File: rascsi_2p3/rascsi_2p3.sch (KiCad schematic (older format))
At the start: 90 parts, among them IC1 SN74LS641-1DW, IC2 SN74LS641-1DW, IC3 SN74LS641-1DW, IC4 SN74LS641-1DW, J1 Raspberry_Pi_2_3, J2 Conn_01x02_Male, J3 Conn_02x25_Odd_Even, J4 I2C Pinout, J5 Conn_02x03_Odd_Even, J6 CONNFLY DB-25, J7 Conn_01x02_Male, X1 Mac, X2 Dogcow, X3 Mac, X4 Dogcow, X5 Dogcow, X6 Dogcow, X7 Pi, X8 Pi

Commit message: Commit ordered version of the board
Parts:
- D1, D2, D3, D4: Description (none) -> Generic 0805 Green LED
- H1, H2, H3, H4, H5, H6: Description (none) -> N/A - Mounting Hole; Height (none) -> N/A; LCSC (none) -> N/A; Manufacturer_Name (none) -> N/A; Manufacturer_Part_Number (none) -> N/A; Mouser Part Number (none) -> N/A; Mouser Price/Stock (none) -> N/A
- IC1, IC2, IC3, IC4: footprint SOIC127P1030X265-20N -> SamacSys_Parts:SOIC127P1030X265-20N
- J2, J7: value Conn_01x02_Male -> DNP; Description (none) -> DNP; Height (none) -> DNP; LCSC C2337 -> DNP; Manufacturer_Name (none) -> DNP; Manufacturer_Part_Number (none) -> DNP; Mouser Part Number (none) -> DNP; Mouser Price/Stock (none) -> DNP
- J3: Description (none) -> 2.54mm 2x25 pin Box Header; Manufacturer_Name (none) -> TE Connectivity; Manufacturer_Part_Number (none) -> 3-1761603-5; Mouser Part Number (none) -> 571-3-1761603-5; Mouser Price/Stock (none) -> https://www.mouser.com/ProductDetail/TE-Connectivity/3-1761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
- J4: Description (none) -> Generic 1x5 2.5mm pin socket; Manufacturer_Name (none) -> Harwin; Manufacturer_Part_Number (none) -> M20-7820546; Mouser Part Number (none) -> 855-M20-7820546; Mouser Price/Stock (none) -> https://www.mouser.com/ProductDetail/Harwin/M20-7820546?qs=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
- J5: value Conn_02x03_Odd_Even -> DNP; Description (none) -> DNP; Height (none) -> DNP; LCSC C3409 -> DNP; Manufacturer_Name (none) -> DNP; Manufacturer_Part_Number (none) -> DNP; Mouser Part Number (none) -> DNP; Mouser Price/Stock (none) -> DNP
- J6: footprint L717SDB25PA4CH4F -> SamacSys_Parts:L717SDB25PA4CH4F
- R1, R10, R11, R12, R13, R14, R15, R16, R17, R18, R19, R2, R20, R21, R22, R23, R24, R25, R26, R27, R28, R29, R3, R30, R31, R32, R33, R34, R35, R36, R37, R38, R39, R4, R40, R41, R42, R43, R44, R45, R46, R47, R48, R49, R5, R50, R51, R52, R53, R54, R55, R56, R57, R58, R6, R7, R8, R9: footprint Resistor_SMD:R_0402_1005Metric -> Resistor_THT:R_Axial_DIN0204_L3.6mm_D1.6mm_P1.90mm_Vertical
- X1, X2, X3, X4, X5, X6, X7, X8: Description (none) -> N/A - Silkscreen; Height (none) -> N/A; LCSC (none) -> N/A; Manufacturer_Name (none) -> N/A; Manufacturer_Part_Number (none) -> N/A; Mouser Part Number (none) -> N/A; Mouser Price/Stock (none) -> N/A
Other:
- note added: "2.3a"
- note removed: "2.3"

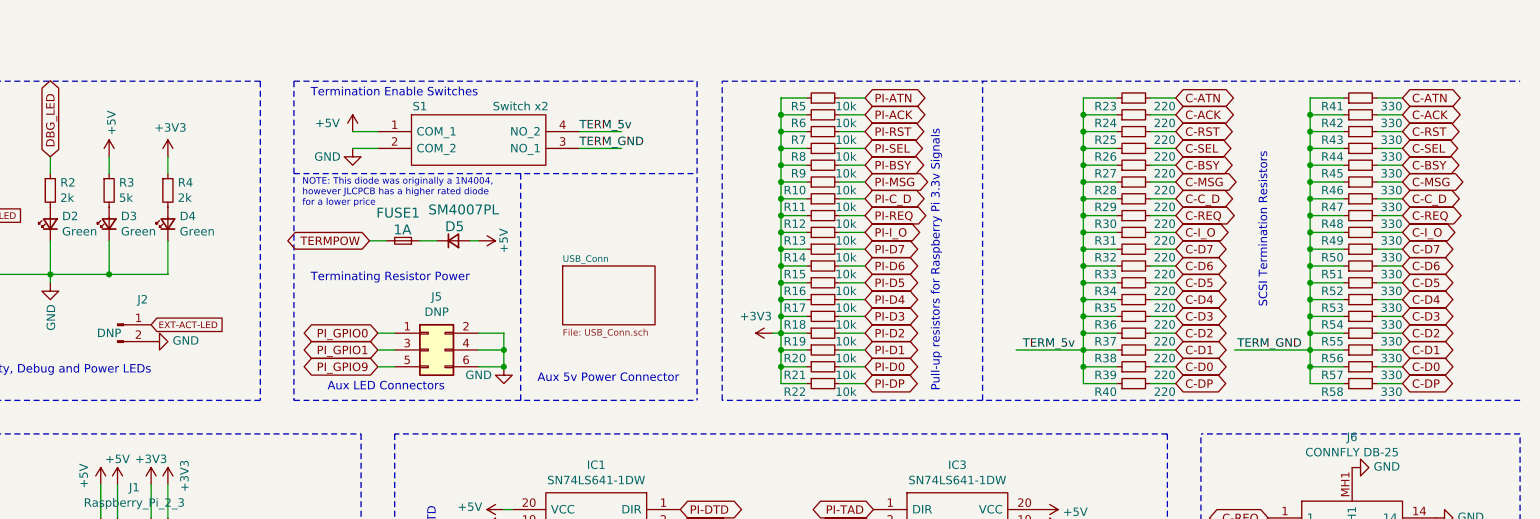
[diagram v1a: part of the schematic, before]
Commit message: Updated to correct part fields and descriptions. Removed conflicting mouser references
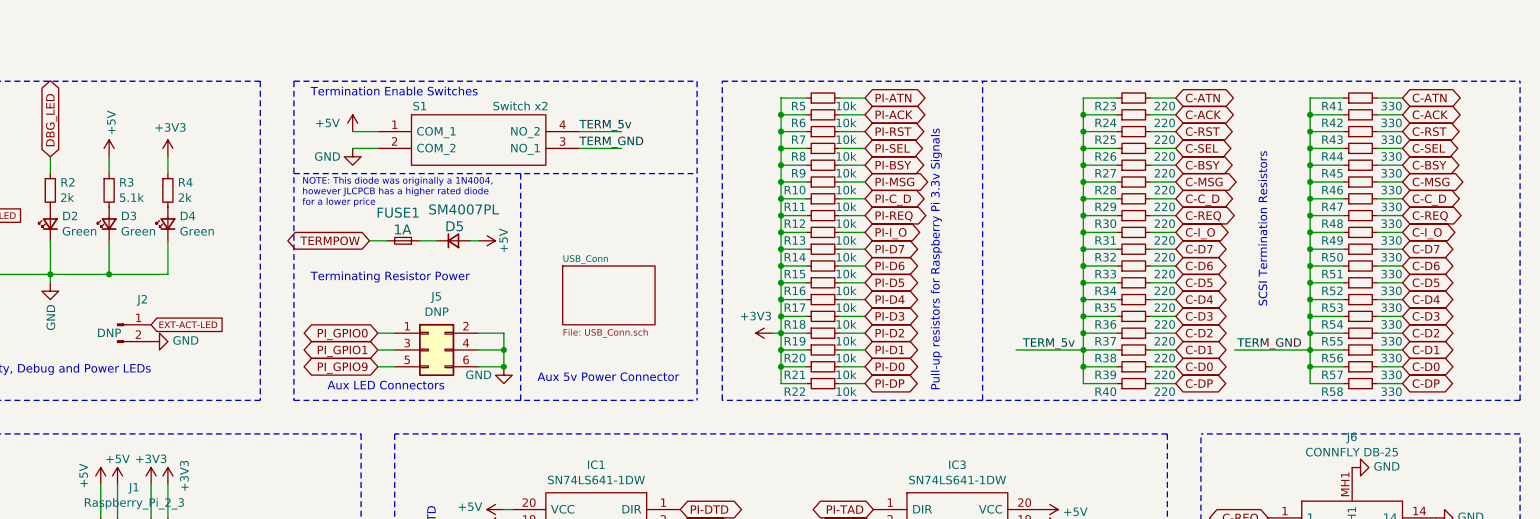
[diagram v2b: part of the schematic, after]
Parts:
- D1, D2, D3, D4: Description Generic 0805 Green LED -> 0805 Light Emitting Diodes (LED) RoHS; Manufacturer_Name (none) -> Hubei KENTO Elec; Manufacturer_Part_Number (none) -> C2297
- D5: Description (none) -> 1kV 1A 1.1V @ 1A SOD-123FL Diodes - General Purpose RoHS; Manufacturer_Name (none) -> MDD(Microdiode Electronics); Manufacturer_Part_Number (none) -> SM4007PL
- FUSE1: Description (none) -> SMD Fuse Fast Blow 1A 50A 0.0062 SMD1206 Surface Mount Fuses; Manufacturer_Name (none) -> Shenzhen lanson Elec; Manufacturer_Part_Number (none) -> 12B1100B
- H1, H2, H3, H4, H5, H6: Description N/A - Mounting Hole -> DNP; Height N/A -> (none); LCSC N/A -> DNP; Manufacturer_Name N/A -> DNP; Manufacturer_Part_Number N/A -> DNP; Mouser Part Number N/A -> (none); Mouser Price/Stock N/A -> (none)
- IC1, IC2, IC3, IC4: Height 2.65 -> (none); LCSC (none) -> N/A
- J1: Description (none) -> Female Header 40 2 right-angle，180degrees 2.54mm 2.54mm Pin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; Manufacturer_Name (none) -> BOOMELE(Boom Precision Elec); Manufacturer_Part_Number (none) -> C50982
- J2, J5, J7: Height DNP -> (none); Mouser Part Number DNP -> (none); Mouser Price/Stock DNP -> (none)
- J3: Description 2.54mm 2x25 pin Box Header -> Header 50 0.100\"(2.54mm) 2 2.54MM IDC Connectors RoHS; Manufacturer_Name TE Connectivity -> BOOMELE(Boom Precision Elec); Manufacturer_Part_Number 3-1761603-5 -> C30006; Mouser Part Number 571-3-1761603-5 -> (none); Mouser Price/Stock https://www.mouser.com/ProductDetail/TE-Connectivity/3-1761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 -> (none)
- J4: Description Generic 1x5 2.5mm pin socket -> Female Header 5 1 right-angle，180degrees 2.54mm 2.54mm Pin 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; LCSC C2337 -> C50950; Manufacturer_Name Harwin -> BOOMELE(Boom Precision Elec) C50950; Manufacturer_Part_Number M20-7820546 -> C50950; Mouser Part Number 855-M20-7820546 -> (none); Mouser Price/Stock https://www.mouser.com/ProductDetail/Harwin/M20-7820546?qs=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 -> (none)
- J6: Description D-Sub Standard Connectors 25P Size B Stamped Male DSub Cont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 -> D-Sub Receptacle,Female Socket 25 2 1.5A(Contact) Through H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; Height 12.55 -> (none); Manufacturer_Name Amphenol -> CONNFLY Elec; Manufacturer_Part_Number L717SDB25PA4CH4F -> DS1037-25FNAKT74-0CC; Mouser Part Number 523-L717SDB25PA4CH4F -> (none); Mouser Price/Stock https://www.mouser.com/Search/Refine.aspx?Keyword=523-L717S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 -> (none)
- R1, R2, R4: Description (none) -> 2kΩ ±1% 1/16W ±100ppm/℃ 0402 Chip Resistor; Manufacturer_Name (none) -> UNI-ROYAL(Uniroyal Elec); Manufacturer_Part_Number (none) -> 0402WGF2001TCE
- R10, R11, R12, R13, R14, R15, R16, R17, R18, R19, R20, R21, R22, R5, R6, R7, R8, R9: Description (none) -> 10kΩ ±1% 1/16W ±100ppm/℃ 0402 Chip Resistor; Manufacturer_Name (none) -> UNI-ROYAL(Uniroyal Elec); Manufacturer_Part_Number (none) -> 0402WGF1002TCE
- R23, R24, R25, R26, R27, R28, R29, R30, R31, R32, R33, R34, R35, R36, R37, R38, R39, R40: Description (none) -> 220Ω ±1% 1/16W ±100ppm/℃ 0402 Chip Resistor; Manufacturer_Name (none) -> UNI-ROYAL(Uniroyal Elec); Manufacturer_Part_Number (none) -> 0402WGF2200TCE
- R3: value 5k -> 5.1k; Description (none) -> 5.1kΩ ±1% 1/16W ±100ppm/℃ 0402 Chip Resistor; Manufacturer_Name (none) -> UNI-ROYAL(Uniroyal Elec); Manufacturer_Part_Number (none) -> 0402WGF5101TCE
- R41, R42, R43, R44, R45, R46, R47, R48, R49, R50, R51, R52, R53, R54, R55, R56, R57, R58: Description (none) -> 330Ω ±1% 1/16W ±100ppm/℃ 0402 Chip Resistor; Manufacturer_Name (none) -> UNI-ROYAL(Uniroyal Elec); Manufacturer_Part_Number (none) -> 0402WGF3300TCE
- S1: Description DIP Switches / SIP Switches HALF PITCH 2 POS -> SPST 2 1.27mm, Half Slide (Standard) Black SMD DIP Switches; Height 2.3 -> (none); Manufacturer_Part_Number TDA02H0SB1R -> DSHP02TSGET; Mouser Part Number 611-TDA02H0SB1R -> (none); Mouser Price/Stock https://www.mouser.co.uk/ProductDetail/CK/TDA02H0SB1R?qs=%2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 -> (none)
- X1, X2, X3, X4, X5, X6, X7, X8: Height N/A -> (none); Mouser Part Number N/A -> (none); Mouser Price/Stock N/A -> (none)

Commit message: Added STEP file and updated symbol and 3d model references to reference the correct gender of parts. Should be no functional change
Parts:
- J6: footprint SamacSys_Parts:L717SDB25PA4CH4F -> SamacSys_Parts:57489011; symbol SamacSys_Parts:L717SDB25PA4CH4F -> SamacSys_Parts:5748901-1
- R1, R10, R11, R12, R13, R14, R15, R16, R17, R18, R19, R2, R20, R21, R22, R23, R24, R25, R26, R27, R28, R29, R3, R30, R31, R32, R33, R34, R35, R36, R37, R38, R39, R4, R40, R41, R42, R43, R44, R45, R46, R47, R48, R49, R5, R50, R51, R52, R53, R54, R55, R56, R57, R58, R6, R7, R8, R9: footprint Resistor_THT:R_Axial_DIN0204_L3.6mm_D1.6mm_P1.90mm_Vertical -> Resistor_SMD:R_0402_1005Metric
